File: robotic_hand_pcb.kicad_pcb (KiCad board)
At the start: 4 copper layers, 55 x 73.5 mm, 125 parts, among them J1 2171750001, J10 A3, J11 A4, J12 A5, J13 A6, J14 A7, J15 JST 1x5 Male, J16 JST 1x5 Male, J17 JST 1x5 Male, J18 JST 1x5 Male, J19 JST 1x5 Male, J2 TC2050-IDC, J3 Battery, J4 Battery, J6 UART, J7 WS2812B, J8 A1, J9 A2, SW1 SPST, U1 LMR51430, U10 ACS712xLCTR-05B, U11 ACS712xLCTR-05B, U12 ACS712xLCTR-05B, U13 ACS712xLCTR-05B, U14 ULN2003ADR, U15 ULN2003ADR, U16 ULN2003ADR, U17 ULN2003ADR, U18 ULN2003ADR, U2 ld39150dt33-r, U3 TXB0104QPWRQ1, U4 STM32F446RET, U5 VL53L4CD, U7 BNO085, U8 ADS114S08, U9 ACS712xLCTR-05B, Y1 8M, Y2 32k768

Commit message: Cleanup and update docs
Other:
- board text added: "ADC"
- board text added: "Daniel Jeon robotic_hand_pcb v0.1.0"
- board text added: "NRST"
- board text added: "RST"
- board text added: "RX"
- board text added: "STM32F446RE 5V Buck regulator 5x Unipolar stepper driver TOF sensor (VL53L4CD) IMU sensor (BNO085) PWM LEDs (WS2812B) 7x ADC"
- board text added: "TX"

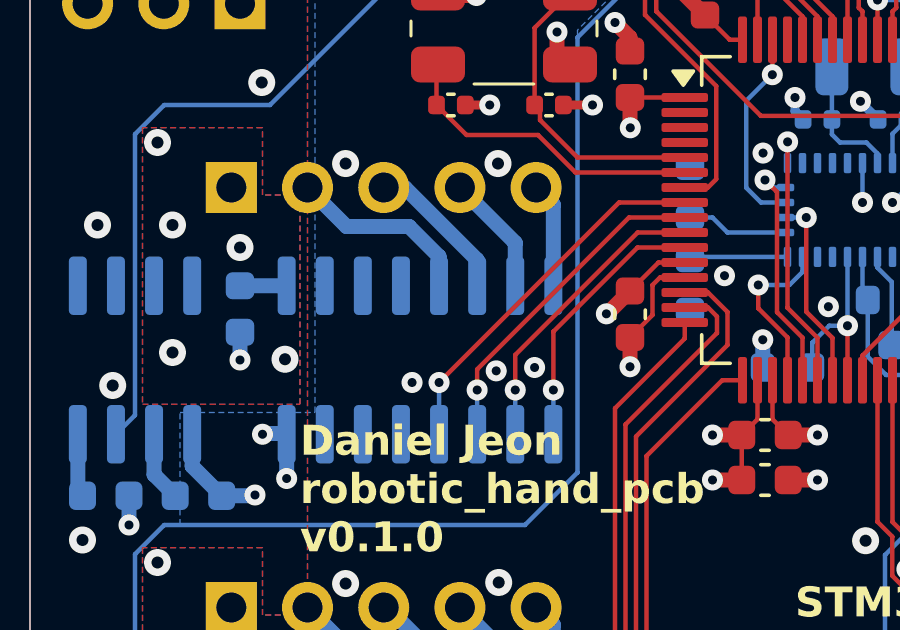
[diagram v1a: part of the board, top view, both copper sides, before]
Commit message: Add PCBWay logo silkscreen
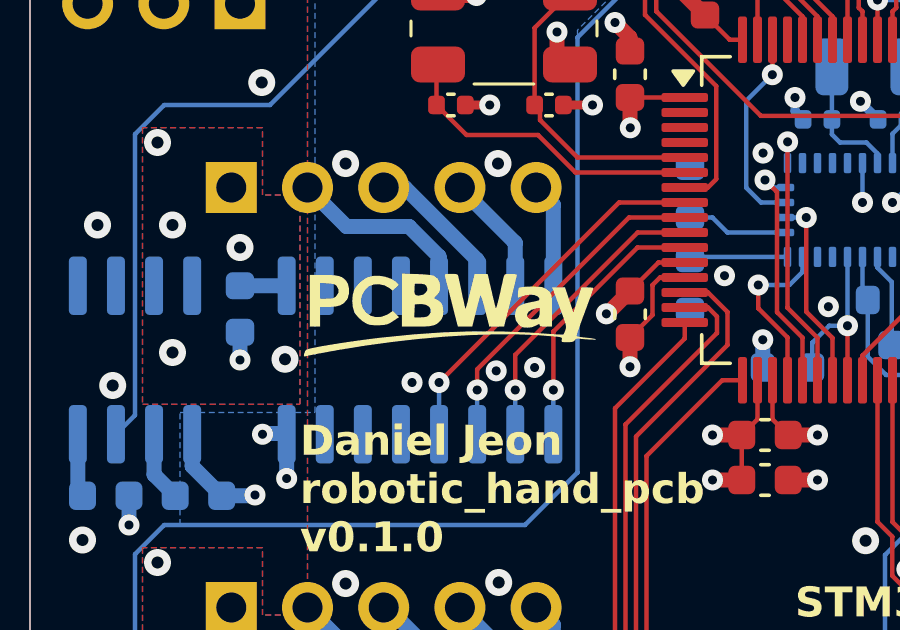
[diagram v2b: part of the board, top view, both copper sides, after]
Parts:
- added G***: LOGO, LOGO, F.Cu at (135.6, 108.4)

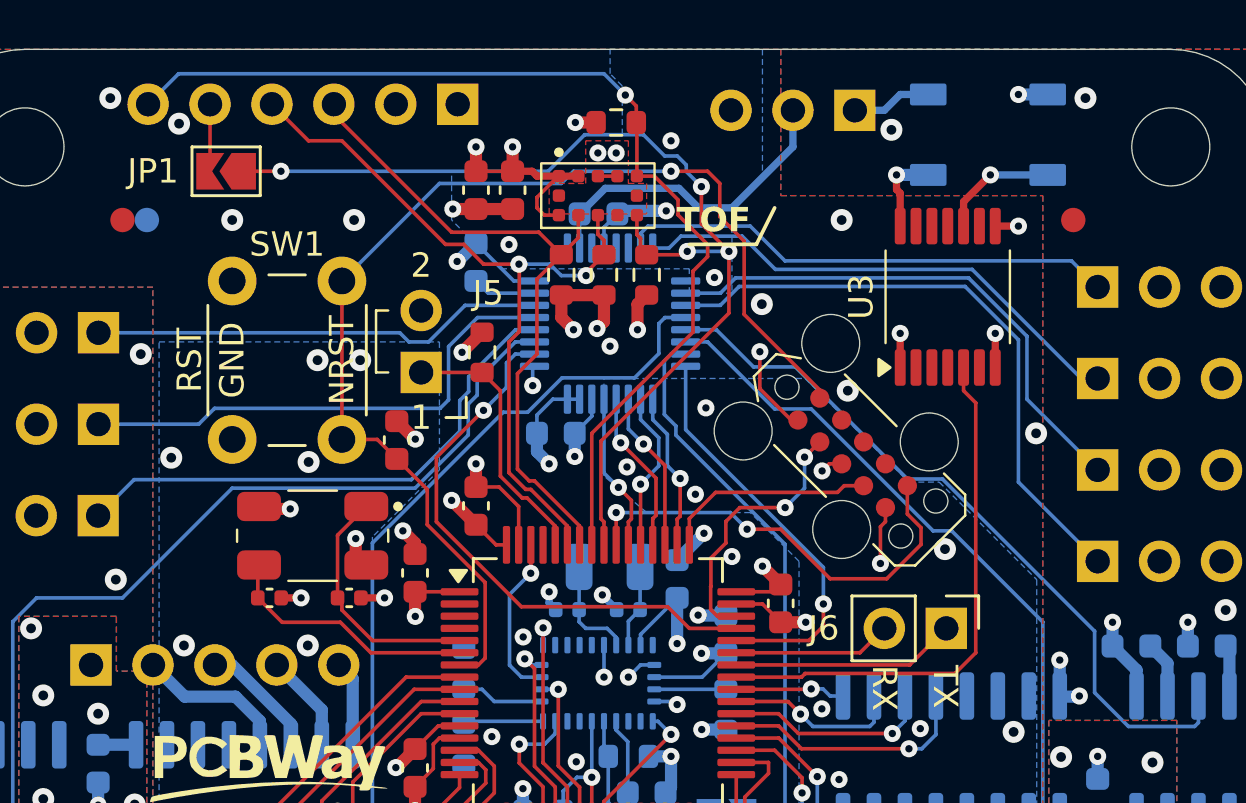
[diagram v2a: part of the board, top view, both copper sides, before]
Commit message: Fix conflicting GPIO EXTI4 usage
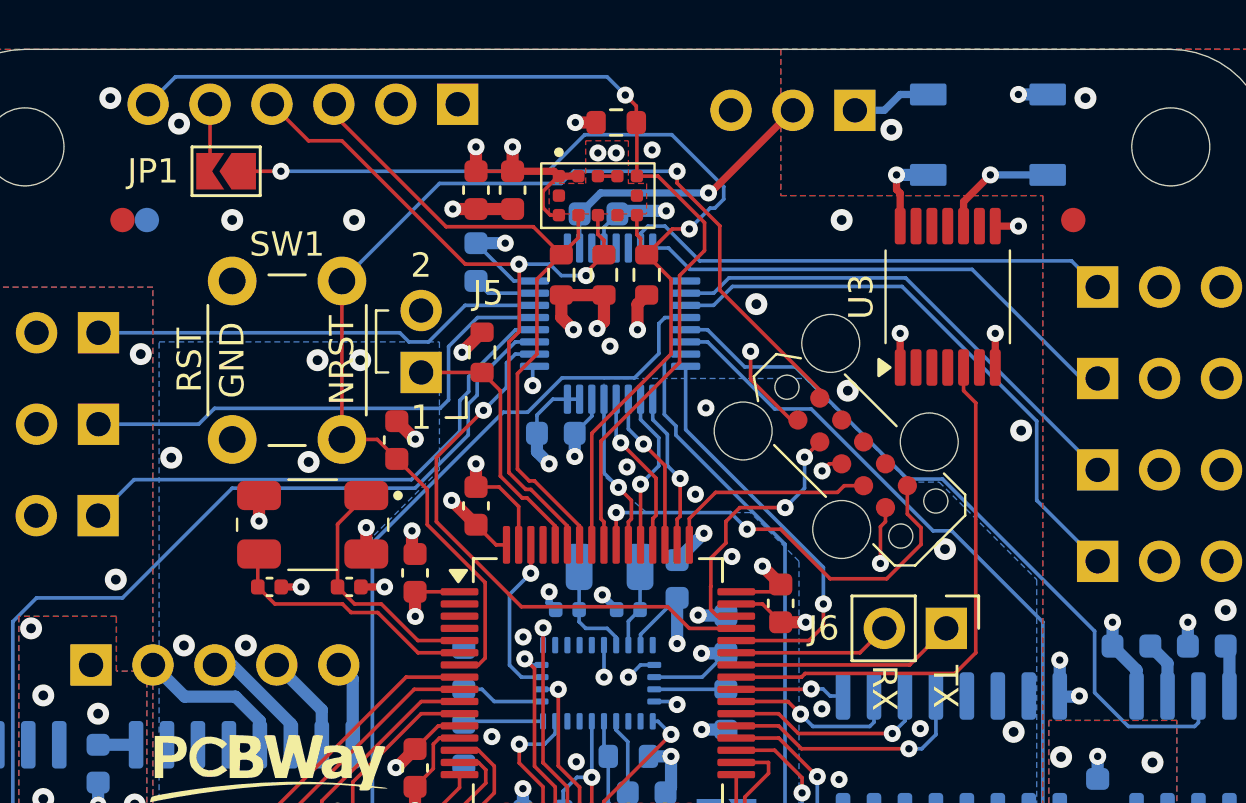
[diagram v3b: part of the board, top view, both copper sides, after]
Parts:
- moved C15 0.45 mm to (138.3, 101.0)
- moved C16 0.45 mm to (135.0, 101.0)
- moved Y1 0.45 mm to (136.8, 98.5)
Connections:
- JP1 pad 1: /EXTI4_TOF_INT -> /EXTI5_TOF_INT
- R9 pad 2: /EXTI4_TOF_INT -> /EXTI5_TOF_INT
- U4 pad 56: /EXTI4_TOF_INT -> /GPIO_TOF_XSHUT
- U4 pad 57: /GPIO_TOF_XSHUT -> /EXTI5_TOF_INT
- U5 pad 7: /EXTI4_TOF_INT -> /EXTI5_TOF_INT
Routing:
- net /EXTI4_TOF_INT: track 42.9 -> 0.00 mm, vias 4 -> 0
- net /EXTI5_TOF_INT: track 0.00 -> 41.2 mm, vias 0 -> 2
- net +5V: track 36.0 -> 34.4 mm, vias 14 -> 15
- net /robotic_hand_pcb_analog/ADC6: track 25.3 -> 23.8 mm
- net /robotic_hand_pcb_analog/ADC7: track 21.9 -> 20.4 mm
- net /NRST: track 47.5 -> 46.8 mm
- net GND: track 104.2 -> 103.6 mm, vias 141 -> 139
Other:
- board text removed: "TOF"

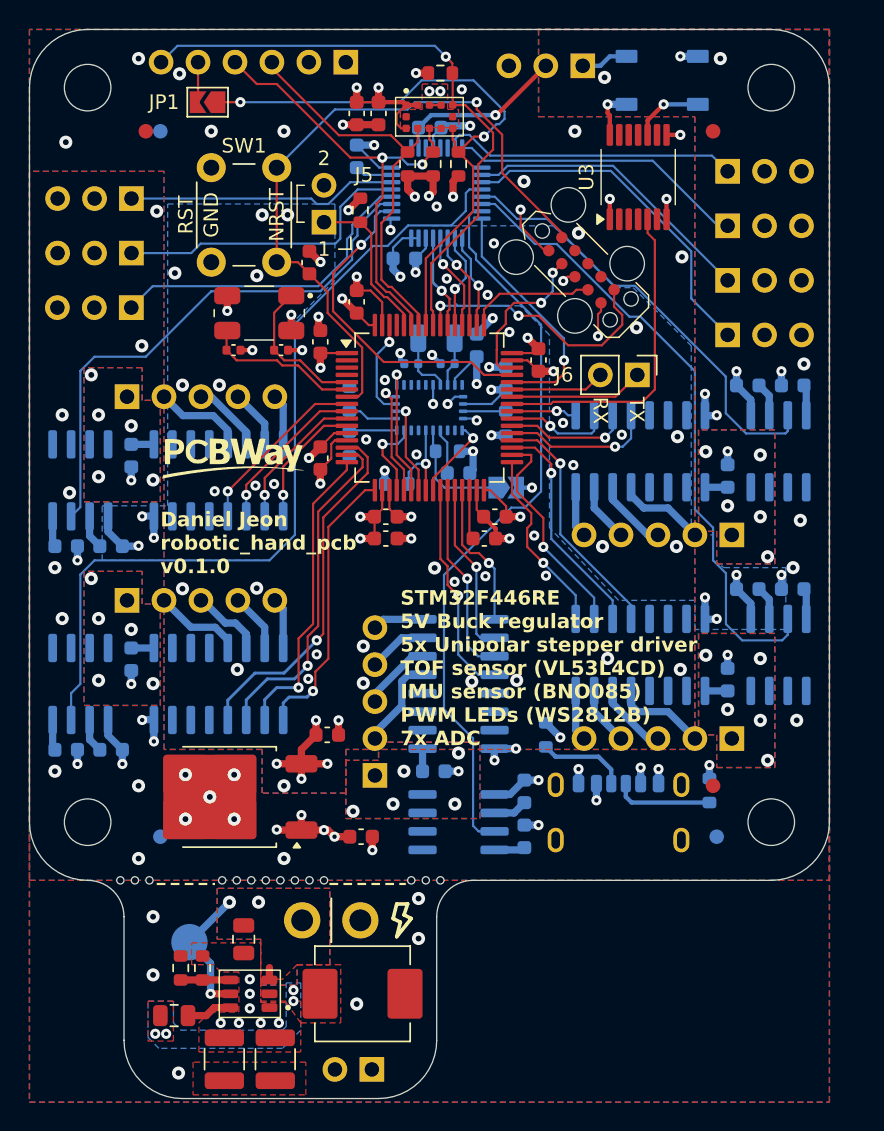
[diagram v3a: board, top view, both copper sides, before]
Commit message: Fix C4 value error and cleanup silkscreen
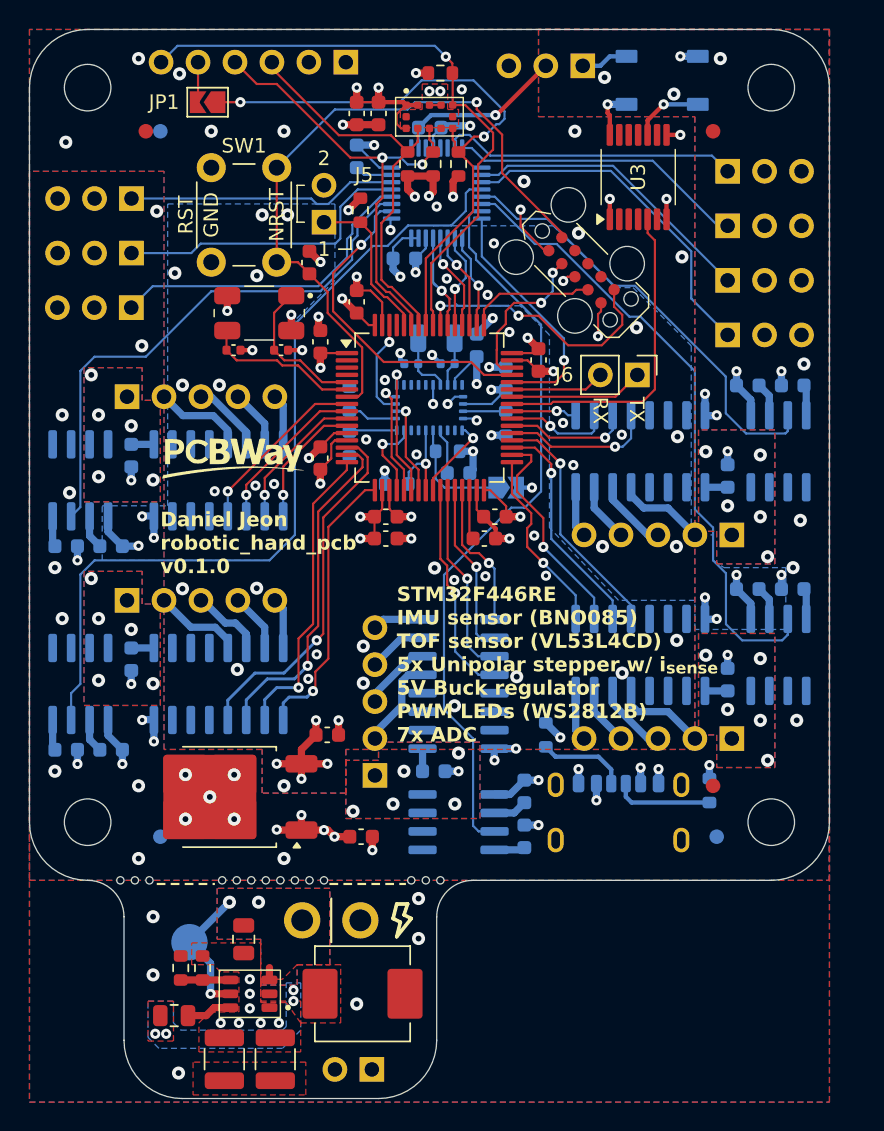
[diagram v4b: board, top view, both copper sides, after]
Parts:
- C4: value 44u -> 22u
- J4: value Battery -> 5V
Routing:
- net GND: vias 139 -> 140
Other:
- board text added: "STM32F446RE IMU sensor (BNO085) TOF sensor (VL53L4CD) 5x Unipolar stepper w/ i_{sense} 5V Buck regulator PWM LEDs (WS2812B) 7x ADC"
- board text removed: "STM32F446RE 5V Buck regulator 5x Unipolar stepper driver TOF sensor (VL53L4CD) IMU sensor (BNO085) PWM LEDs (WS2812B) 7x ADC"
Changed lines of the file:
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@@
 		(at 162.85 89.15 90)
 		(property "Reference" "U3"
-			(at 0 -3.55 90)
+			(at 0 0 90)
 			(unlocked yes)
 			(layer "F.SilkS")
@@
 				(font
 					(size 1 1)
-					(thickness 0.1)
+					(thickness 0.15)
 				)
 			)
@@
 			)
 		)
-		(property "Value" "44u"
+		(property "Value" "22u"
 			(at 0 2.3 90)
 			(layer "F.Fab")
@@
 			)
 		)
-		(property "Value" "Battery"
+		(property "Value" "5V"
 			(at 0 -4.87 90)
 			(layer "B.Fab")
@@
 		)
 	)
-	(gr_text "STM32F446RE\n5V Buck regulator\n5x Unipolar stepper driver\nTOF sensor (VL53L4CD)\nIMU sensor (BNO085)\nPWM LEDs (WS2812B)\n7x ADC"
-		(at 146.5 117.5 0)
+	(gr_text "STM32F446RE\nIMU sensor (BNO085)\nTOF sensor (VL53L4CD)\n5x Unipolar stepper w/ i_{sense}\n5V Buck regulator\nPWM LEDs (WS2812B)\n7x ADC"
+		(at 146.25 117.25 0)
 		(layer "F.SilkS")
 		(effects
@@
 	)
 	(via
-		(at 154.5 123.75)
+		(at 154.5 123.5)
 		(size 0.9)
 		(drill 0.4)
@@
 	)
 	(via
+		(at 165.307109 83.442891)
+		(size 0.9)
+		(drill 0.4)
+		(layers "F.Cu" "B.Cu")
+		(remove_unused_layers yes)
+		(keep_end_layers no)
+		(free yes)
+		(zone_layer_connections "In1.Cu" "In2.Cu")
+		(net 2)
+	)
+	(via
 		(at 168.25 105.525)
 		(size 0.7)
@@
 	)
 	(via
-		(at 150.228205 116.973556)
+		(at 150.205824 116.852225)
 		(size 0.7)
 		(drill 0.3)
@@
 	)
 	(via
-		(at 151.412439 123.832313)
+		(at 150.225 125.5)
 		(size 0.9)
 		(drill 0.4)
@@
 	)
 	(via
-		(at 165.75 123)
+		(at 165.5 121)
 		(size 0.9)
 		(drill 0.4)
@@
 	)
 	(via
-		(at 160.75 122.25)
+		(at 161.75 123.25)
 		(size 0.9)
 		(drill 0.4)
@@
 		(drill 0.4)
 		(layers "F.Cu" "B.Cu")
+		(remove_unused_layers yes)
+		(keep_end_layers no)
 		(free yes)
+		(zone_layer_connections "F.Cu" "B.Cu")
 		(net 4)
 	)
@@
 		(drill 0.4)
 		(layers "F.Cu" "B.Cu")
+		(remove_unused_layers yes)
+		(keep_end_layers no)
 		(free yes)
+		(zone_layer_connections "F.Cu" "B.Cu")
 		(net 4)
 	)
@@
 		(drill 0.4)
 		(layers "F.Cu" "B.Cu")
+		(remove_unused_layers yes)
+		(keep_end_layers no)
 		(free yes)
+		(zone_layer_connections "F.Cu" "B.Cu")
 		(net 4)
 	)
@@
 		(drill 0.3)
 		(layers "F.Cu" "B.Cu")
+		(remove_unused_layers yes)
+		(keep_end_layers no)
+		(zone_layer_connections)
 		(net 4)
 	)
@@
 		(drill 0.4)
 		(layers "F.Cu" "B.Cu")
+		(remove_unused_layers yes)
+		(keep_end_layers no)
 		(free yes)
+		(zone_layer_connections "F.Cu" "B.Cu")
 		(net 4)
 	)
@@
 		(drill 0.4)
 		(layers "F.Cu" "B.Cu")
+		(remove_unused_layers yes)
+		(keep_end_layers no)
 		(free yes)
+		(zone_layer_connections "F.Cu" "B.Cu")
 		(net 4)
 	)
@@
 		(drill 0.4)
 		(layers "F.Cu" "B.Cu")
+		(remove_unused_layers yes)
+		(keep_end_layers no)
 		(free yes)
+		(zone_layer_connections "F.Cu" "B.Cu")
 		(net 4)
 	)
@@
 		(drill 0.4)
 		(layers "F.Cu" "B.Cu")
+		(remove_unused_layers yes)
+		(keep_end_layers no)
 		(free yes)
+		(zone_layer_connections "F.Cu" "B.Cu")
 		(net 4)
 	)
@@
 		(drill 0.3)
 		(layers "F.Cu" "B.Cu")
+		(remove_unused_layers yes)
+		(keep_end_layers no)
+		(zone_layer_connections)
 		(net 42)
 	)
@@
 	)
 	(segment
-		(start 150.475 117.9263)
-		(end 149.743205 117.194505)
+		(start 149.720824 115.865798)
+		(end 149.25 115.394974)
 		(width 0.15)
 		(layer "F.Cu")
@@
 	)
 	(segment
-		(start 149.743205 115.888179)
-		(end 149.25 115.394974)
+		(start 149.25 115.394974)
+		(end 149.25 110.675)
 		(width 0.15)
 		(layer "F.Cu")
@@
 	)
 	(segment
-		(start 149.25 115.394974)
-		(end 149.25 110.675)
+		(start 150.269105 117.75)
+		(end 149.720824 117.201719)
 		(width 0.15)
 		(layer "F.Cu")
@@
 	)
 	(segment
-		(start 149.743205 117.194505)
-		(end 149.743205 115.888179)
+		(start 149.720824 117.201719)
+		(end 149.720824 115.865798)
 		(width 0.15)
 		(layer "F.Cu")
@@
 	)
 	(via
-		(at 150.475 117.9263)
+		(at 150.269105 117.75)
 		(size 0.7)
 		(drill 0.3)
@@
 	)
 	(segment
-		(start 152.975 123.365)
-		(end 151.865 123.365)
+		(start 151.865 123.365)
+		(end 152.975 123.365)
 		(width 0.15)
 		(layer "B.Cu")
@@
 	)
 	(segment
-		(start 151.865 123.365)
-		(end 150.475 121.975)
+		(start 150.269105 117.75)
+		(end 150.269105 121.769105)
 		(width 0.15)
 		(layer "B.Cu")
@@
 	)
 	(segment
-		(start 150.475 121.975)
-		(end 150.475 117.9263)
+		(start 150.269105 121.769105)
+		(end 151.865 123.365)
 		(width 0.15)
 		(layer "B.Cu")
@@
 			"4ab33b46-e66b-4c21-987d-250bcf2de26f" "4b0fb7bd-5d98-47b9-a462-f54429e85015"
 			"686d9aba-e3b3-4ebe-86e7-59773e62a924" "6ef3929f-0a36-4a7b-9143-554193311425"
-			"737e30cd-a12c-4809-9a97-962862eae9fb" "74044169-69f0-48c8-899c-00c31efe1927"
-			"7be9ae65-13b0-4540-80b8-f23c78206dd5" "7f9b859c-0ad7-4431-998a-1b8d5433f98a"
-			"81fbf83d-7253-4cf6-80e2-3cc74a9f1be9" "8a6a085d-a36b-48fb-ab6f-176315eb0cde"
-			"8bc553be-960b-4cbe-8fd2-3c3f1fe60a48" "8c1c293c-c2d5-42d2-a084-9f0d42bf3489"
-			"8d438d7a-ea75-4ea7-a915-94100e167ceb" "a47890d5-db6b-44e0-b78b-359531fae334"
-			"acb3e047-a7fa-48eb-aacb-c4bb3820ddfa" "bd429b58-1012-4966-8897-1a64d7f04997"
-			"be608de1-0bae-4e43-9f31-d3127c189e31" "bfeaaadc-137b-4c4f-897d-75edc98467ea"
-			"c00e919e-0a02-460a-b90b-2c160d454b3e" "c80d7877-a371-4dd6-adb5-8b0deb344384"
-			"c8bf72c2-dc8b-430f-9a7d-c03c15d88aad" "cfe1f4f8-67ce-485c-811d-139a6a73b28b"
-			"d82dc307-bd64-447b-beea-df629b8637af" "dfac07d4-8556-4f40-a579-f273abda1a31"
-			"e55bd235-cb21-44d6-892e-c095f274343a" "eccb20a6-5318-44f2-a6f4-48bc30520464"
-			"edaf256d-c131-4804-b8a8-506cc4ef14e0" "edc110a2-0c88-4914-9ed9-4816ef08e63e"
-			"f0c2bf66-badc-41d2-bd77-cc3be38f75c3" "fa868108-63c4-44e4-b3e3-fb5d3afd1e1a"
-			"faba847a-6f15-4f6c-90a7-d443da52dca0"
+			"6f0f6c93-078f-4514-877a-245d12bf5a7f" "737e30cd-a12c-4809-9a97-962862eae9fb"
+			"74044169-69f0-48c8-899c-00c31efe1927" "7be9ae65-13b0-4540-80b8-f23c78206dd5"
+			"7f9b859c-0ad7-4431-998a-1b8d5433f98a" "81fbf83d-7253-4cf6-80e2-3cc74a9f1be9"
+			"8a6a085d-a36b-48fb-ab6f-176315eb0cde" "8bc553be-960b-4cbe-8fd2-3c3f1fe60a48"
+			"8c1c293c-c2d5-42d2-a084-9f0d42bf3489" "8d438d7a-ea75-4ea7-a915-94100e167ceb"
+			"a47890d5-db6b-44e0-b78b-359531fae334" "acb3e047-a7fa-48eb-aacb-c4bb3820ddfa"
+			"bd429b58-1012-4966-8897-1a64d7f04997" "be608de1-0bae-4e43-9f31-d3127c189e31"
+			"bfeaaadc-137b-4c4f-897d-75edc98467ea" "c00e919e-0a02-460a-b90b-2c160d454b3e"
+			"c80d7877-a371-4dd6-adb5-8b0deb344384" "c8bf72c2-dc8b-430f-9a7d-c03c15d88aad"
+			"cfe1f4f8-67ce-485c-811d-139a6a73b28b" "d82dc307-bd64-447b-beea-df629b8637af"
+			"dfac07d4-8556-4f40-a579-f273abda1a31" "e55bd235-cb21-44d6-892e-c095f274343a"
+			"eccb20a6-5318-44f2-a6f4-48bc30520464" "edaf256d-c131-4804-b8a8-506cc4ef14e0"
+			"edc110a2-0c88-4914-9ed9-4816ef08e63e" "f0c2bf66-badc-41d2-bd77-cc3be38f75c3"
+			"fa868108-63c4-44e4-b3e3-fb5d3afd1e1a" "faba847a-6f15-4f6c-90a7-d443da52dca0"
 		)
 	)

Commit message: Update revision number
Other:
- board text added: "Daniel Jeon robotic_hand_pcb v0.1.1"
- board text removed: "Daniel Jeon robotic_hand_pcb v0.1.0"
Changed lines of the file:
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@@
 	(title_block
 		(title "Robotic Hand PCB")
-		(rev "v0.1.0")
+		(rev "0.1.1")
 		(company "Daniel Jeon")
 	)
@@
 		)
 	)
-	(gr_text "Daniel Jeon\nrobotic_hand_pcb\nv0.1.0"
+	(gr_text "Daniel Jeon\nrobotic_hand_pcb\nv0.1.1"
 		(at 130 116.5 0)
 		(layer "F.SilkS")

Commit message: Fix ADC IC decoupling
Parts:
- C25: value 100n -> 330n
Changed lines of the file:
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@@
 			)
 		)
-		(property "Value" "100n"
+		(property "Value" "330n"
 			(at 0 -1.43 0)
 			(layer "B.Fab")

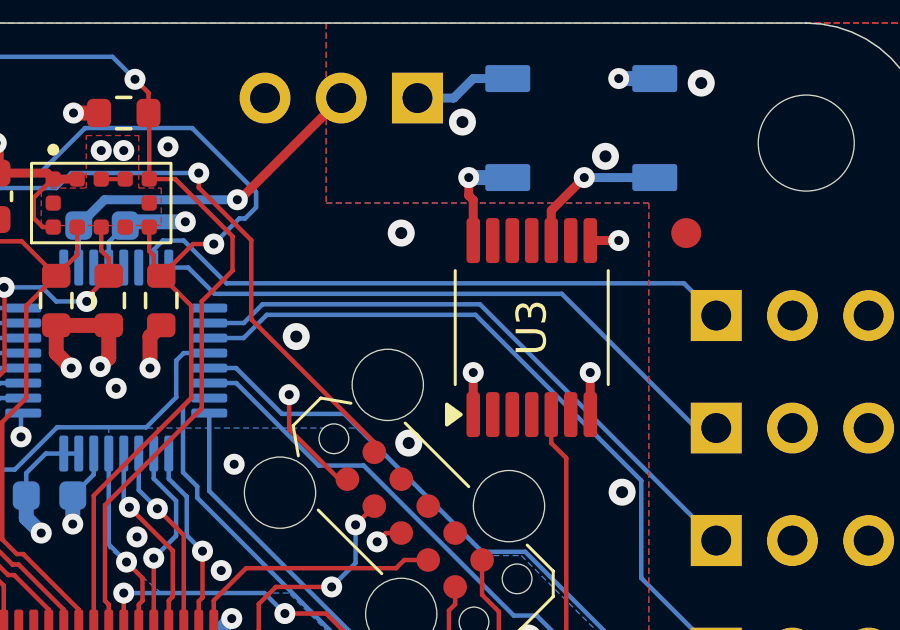
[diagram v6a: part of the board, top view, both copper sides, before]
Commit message: Utilize AINCOM
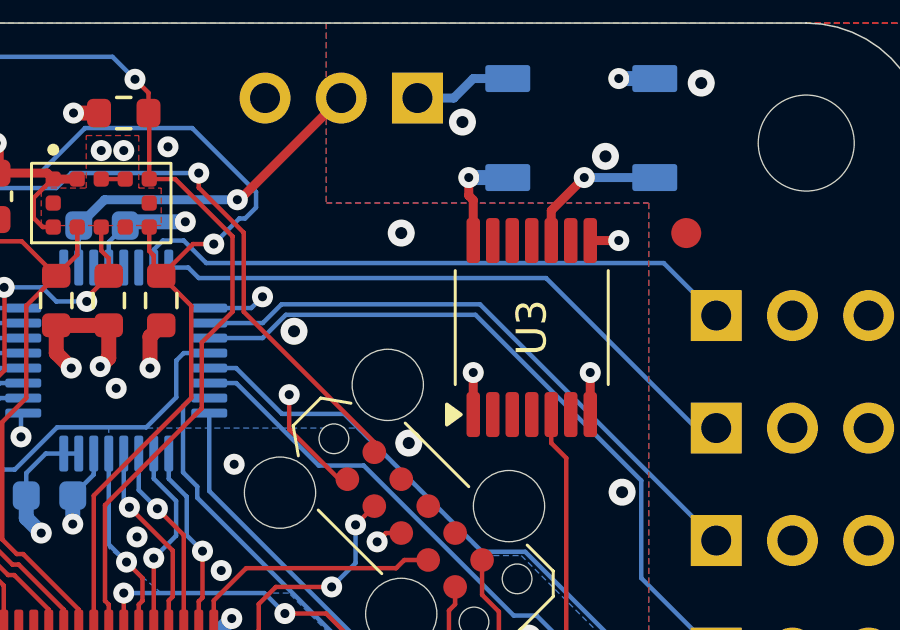
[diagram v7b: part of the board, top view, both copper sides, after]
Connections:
- U8 pad 1: unconnected-(U8-AINCOM-Pad1) -> GND
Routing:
- net GND: track 103.6 -> 105.6 mm, vias 140 -> 141
